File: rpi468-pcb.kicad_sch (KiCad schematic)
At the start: 11 parts, among them J1 USB_A, J2 USB_C_Receptacle_USB2.0, J3 Conn_01x04_Female, U1 LM397

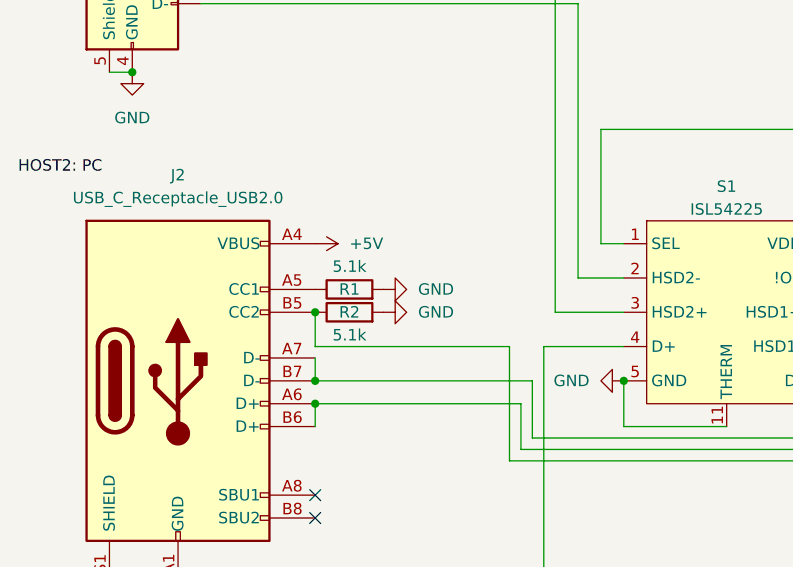
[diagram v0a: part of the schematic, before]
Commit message: bridging CC1 and CC2
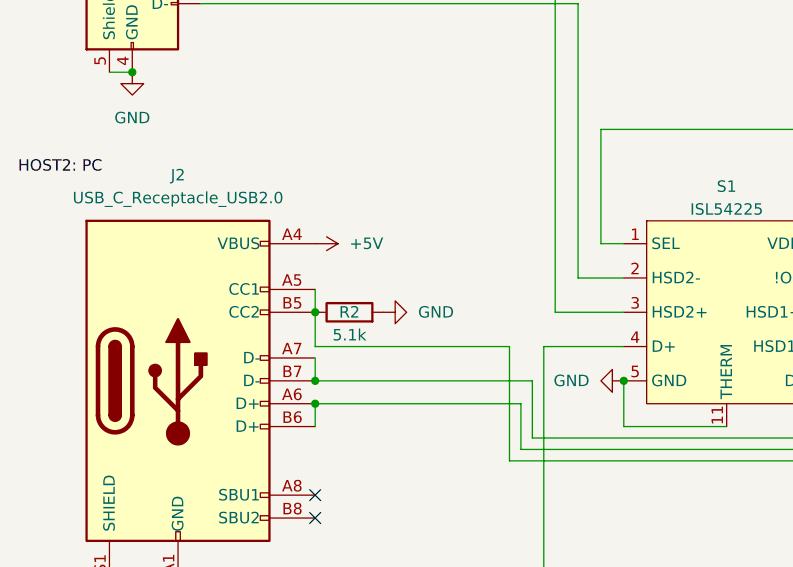
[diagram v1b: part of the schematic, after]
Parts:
- removed R1: 5.1k, Resistor_SMD:R_0603_1608Metric_Pad0.98x0.95mm_HandSolder, symbol Device:R
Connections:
- net at J2.B5 (CC2), R2.1, U1.1 (-): now also J2.A5 (CC1)
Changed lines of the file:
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@@
+    (stroke (width 0) (type default) (color 0 0 0 0))
+  )
+  (wire (pts (xy 100.33 86.36) (xy 100.33 88.9))
     (stroke (width 0) (type default) (color 0 0 0 0))
   )
@@
     (pin "4")
     (pin "5")
-  )
-  (symbol (lib_id "power:GND") (at 107.95 86.36 90) (unit 1)
-    (in_bom yes) (on_board yes) (fields_autoplaced)
-    (property "Reference" "#PWR05" (id 0) (at 114.3 86.36 0)
-      (effects (font (size 1.27 1.27)) hide)
-    )
-    (property "Value" "GND" (id 1) (at 111.76 86.3599 90)
-      (effects (font (size 1.27 1.27)) (justify right))
-    )
-    (property "Footprint" "" (id 2) (at 107.95 86.36 0)
-      (effects (font (size 1.27 1.27)) hide)
-    )
-    (property "Datasheet" "" (id 3) (at 107.95 86.36 0)
-      (effects (font (size 1.27 1.27)) hide)
-    )
-    (pin "1")
   )
   (symbol (lib_id "power:GND") (at 134.62 96.52 270) (unit 1)
@@
     (pin "1")
   )
-  (symbol (lib_id "Device:R") (at 104.14 86.36 90) (unit 1)
-    (in_bom yes) (on_board yes)
-    (property "Reference" "R1" (id 0) (at 104.14 86.36 90))
-    (property "Value" "5.1k" (id 1) (at 104.14 83.82 90))
-    (property "Footprint" "Resistor_SMD:R_0603_1608Metric_Pad0.98x0.95mm_HandSolder" (id 2) (at 104.14 88.138 90)
-      (effects (font (size 1.27 1.27)) hide)
-    )
-    (property "Datasheet" "~" (id 3) (at 104.14 86.36 0)
-      (effects (font (size 1.27 1.27)) hide)
-    )
-    (pin "1")
-    (pin "2")
-  )
   (symbol (lib_id "Comparator:LM397") (at 212.09 87.63 0) (unit 1)
     (in_bom yes) (on_board yes)
@@
       (reference "#PWR04") (unit 1) (value "+5V") (footprint "")
     )
-    (path "/add2d16d-0672-41e4-9648-c6b1b11eedb1"
-      (reference "#PWR05") (unit 1) (value "GND") (footprint "")
-    )
     (path "/8302c781-93fc-4971-b89b-aa336a815fd2"
       (reference "#PWR06") (unit 1) (value "GND") (footprint "")
@@
       (reference "J3") (unit 1) (value "Conn_01x04_Female") (footprint "Connector_PinHeader_1.00mm:PinHeader_1x04_P1.00mm_Vertical")
     )
-    (path "/f619ccc9-65b6-46d1-9876-505c58d8035a"
-      (reference "R1") (unit 1) (value "5.1k") (footprint "Resistor_SMD:R_0603_1608Metric_Pad0.98x0.95mm_HandSolder")
-    )
     (path "/2fa03c2b-51fc-4456-bdb0-f263cbb97ec2"

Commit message: updated pcb
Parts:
- J3: footprint Connector_PinHeader_1.00mm:PinHeader_1x04_P1.00mm_Vertical -> Connector_JST:JST_SH_BM04B-SRSS-TB_1x04-1MP_P1.00mm_Vertical
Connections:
- net at S1.4 (D+): now also J3.2 (Pin_2); no longer J3.3 (Pin_3)
- net at S1.6 (D-): now also J3.3 (Pin_3); no longer J3.2 (Pin_2)
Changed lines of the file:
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@@
-    (stroke (width 0) (type default) (color 0 0 0 0))
-  )
-  (wire (pts (xy 137.16 138.43) (xy 140.97 138.43))
-    (stroke (width 0) (type default) (color 0 0 0 0))
-  )
-  (wire (pts (xy 125.73 140.97) (xy 140.97 140.97))
     (stroke (width 0) (type default) (color 0 0 0 0))
   )
@@
     (stroke (width 0) (type default) (color 0 0 0 0))
   )
+  (wire (pts (xy 137.16 140.97) (xy 140.97 140.97))
+    (stroke (width 0) (type default) (color 0 0 0 0))
+  )
   (wire (pts (xy 157.48 96.52) (xy 157.48 125.73))
     (stroke (width 0) (type default) (color 0 0 0 0))
@@
     (stroke (width 0) (type default) (color 0 0 0 0))
   )
-  (wire (pts (xy 125.73 92.71) (xy 125.73 140.97))
+  (wire (pts (xy 125.73 92.71) (xy 125.73 138.43))
     (stroke (width 0) (type default) (color 0 0 0 0))
   )
@@
     (stroke (width 0) (type default) (color 0 0 0 0))
   )
+  (wire (pts (xy 125.73 138.43) (xy 140.97 138.43))
+    (stroke (width 0) (type default) (color 0 0 0 0))
+  )
   (wire (pts (xy 129.54 85.09) (xy 134.62 85.09))
     (stroke (width 0) (type default) (color 0 0 0 0))
   )
-  (wire (pts (xy 137.16 125.73) (xy 137.16 138.43))
+  (wire (pts (xy 137.16 125.73) (xy 137.16 140.97))
     (stroke (width 0) (type default) (color 0 0 0 0))
   )
@@
       (effects (font (size 1.27 1.27)) (justify left))
     )
-    (property "Footprint" "Connector_PinHeader_1.00mm:PinHeader_1x04_P1.00mm_Vertical" (id 2) (at 146.05 138.43 0)
+    (property "Footprint" "Connector_JST:JST_SH_BM04B-SRSS-TB_1x04-1MP_P1.00mm_Vertical" (id 2) (at 146.05 138.43 0)
       (effects (font (size 1.27 1.27)) hide)
     )
@@
     )
     (path "/e68b378b-715b-4790-8da2-8ea2e44dd6a6"
-      (reference "J3") (unit 1) (value "Conn_01x04_Female") (footprint "Connector_PinHeader_1.00mm:PinHeader_1x04_P1.00mm_Vertical")
+      (reference "J3") (unit 1) (value "Conn_01x04_Female") (footprint "Connector_JST:JST_SH_BM04B-SRSS-TB_1x04-1MP_P1.00mm_Vertical")
     )
     (path "/2fa03c2b-51fc-4456-bdb0-f263cbb97ec2"
